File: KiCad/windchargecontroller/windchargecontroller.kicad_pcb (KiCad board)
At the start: 2 copper layers, 151.9 x 68.6 mm, 55 parts, among them J1 1935789, J2 ESQ-120-XX-X-D-XX, J3 1935789, J4 1935789, J5 1935789, J6 1935789, Q1 Si7336ADP, Q10 2N5087, Q11 Si7336ADP, Q12 Si7336ADP, Q2 Si7336ADP, Q3 Si7336ADP, Q4 2N5210, Q5 2N5087, Q6 Si7336ADP, Q7 2N5210, Q8 2N5087, Q9 2N5210

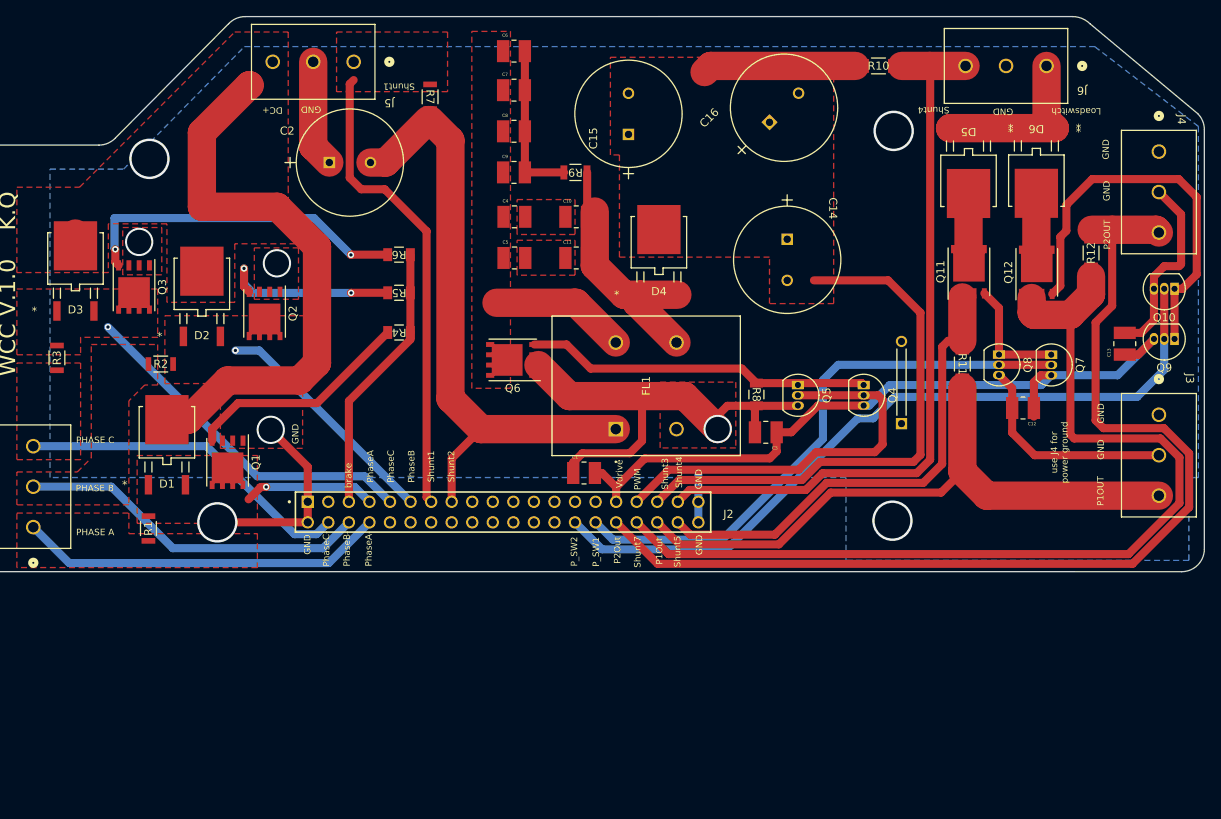
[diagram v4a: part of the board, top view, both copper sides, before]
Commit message: push before i swap out diodes for mosfets
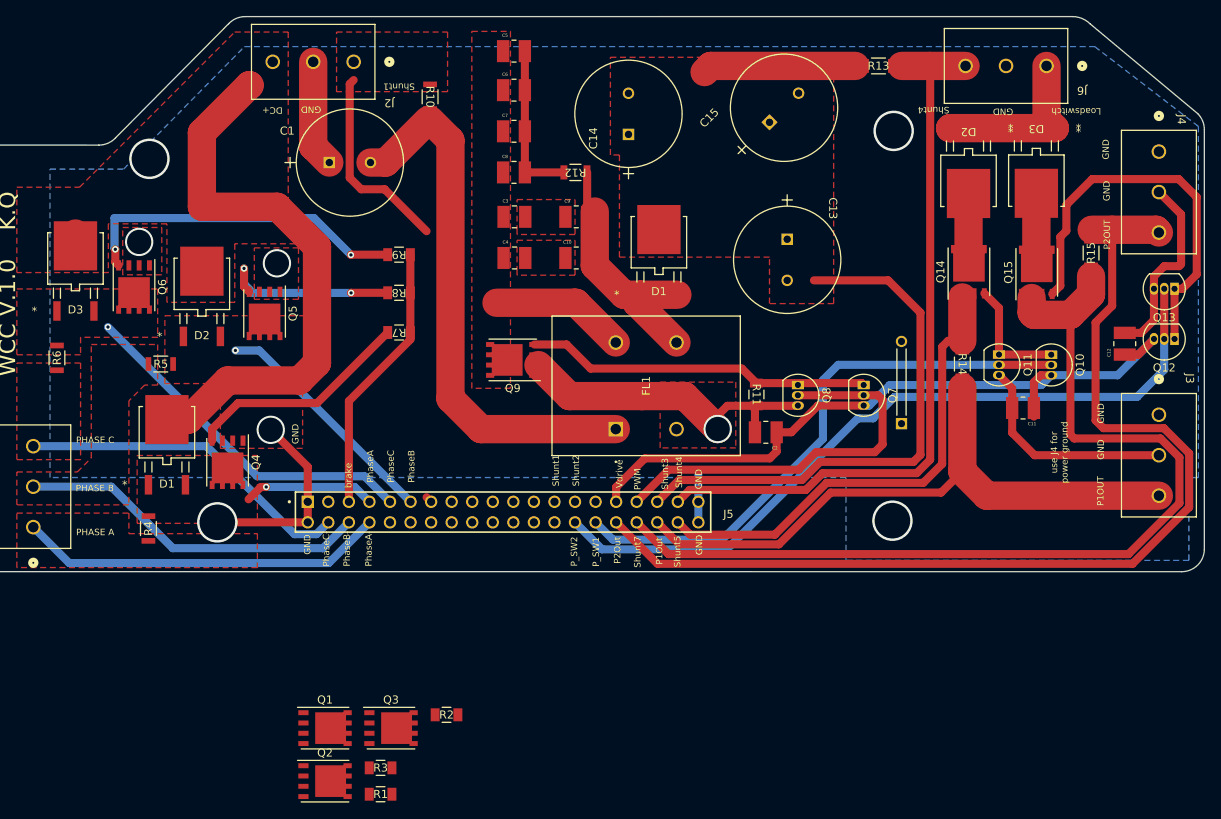
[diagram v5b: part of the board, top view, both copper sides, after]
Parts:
- removed the C1 at (148.2, 89.9)
- added Q1: Si7336ADP, Package_SO:PowerPAK_SO-8_Single, F.Cu at (116.2, 121.4)
- added Q2: Si7336ADP, Package_SO:PowerPAK_SO-8_Single, F.Cu at (116.2, 128.0)
- added Q3: Si7336ADP, Package_SO:PowerPAK_SO-8_Single, F.Cu at (124.3, 121.4)
- added R1: CRCW120616R0FKEA, footprints:RC1206N_VIS, F.Cu at (123.0, 129.6)
- added R2: CRCW120616R0FKEA, footprints:RC1206N_VIS, F.Cu at (131.2, 119.8)
- added R3: CRCW120616R0FKEA, footprints:RC1206N_VIS, F.Cu at (123.0, 126.3)
- renumbered C2 to C1, C11 to C10, C12 to C11, C13 to C12, C14 to C13, C15 to C14, C16 to C15, C3 to C2, C4 to C3, C5 to C4, C6 to C5, C7 to C6, C8 to C7, C9 to C8, C10 to C9, D4 to D1, D5 to D2, D6 to D3, J5 to J2, J2 to J5, Q7 to Q10, Q8 to Q11, Q9 to Q12, Q10 to Q13, Q11 to Q14, Q12 to Q15, Q1 to Q4, Q2 to Q5, Q3 to Q6, Q4 to Q7, Q5 to Q8, Q6 to Q9, R7 to R10, R8 to R11, R9 to R12, R10 to R13, R11 to R14, R12 to R15, R1 to R4, R2 to R5, R3 to R6, R4 to R7, R5 to R8, R6 to R9
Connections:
- J5 pad 13: Shunt1 -> Brake_Q3
- J5 pad 15: Shunt2 -> Brake_Q6
- J5 pad 17: unconnected-(J2-Pad17) -> Brake_Q2
- J5 pad 19: unconnected-(J2-Pad19) -> Brake_Q5
- J5 pad 21: unconnected-(J2-Pad21) -> Brake_Q1
- J5 pad 23: unconnected-(J2-Pad23) -> Brake_Q4
- J5 pad 25: unconnected-(J2-Pad25) -> Shunt1
- J5 pad 27: unconnected-(J2-Pad27) -> Shunt2
- R7 pad 1: Brake_sig -> Brake_Q4
- R8 pad 1: Brake_sig -> Brake_Q5
- R9 pad 1: Brake_sig -> Brake_Q6
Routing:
- net Brake_sig: track 33.7 -> 0.00 mm
- net Brake_Q6: track 0.00 -> 33.7 mm
- net Shunt1: track 58.2 -> 24.5 mm
- net GND: track 152.8 -> 136.4 mm
- net Shunt2: track 77.2 -> 66.8 mm
- net Vdrive: track 91.7 -> 88.4 mm
- net Brake_Q3: track 0.00 -> 0.79 mm
- removed copper zone on F.Cu, net Net-(C9-Pad1)

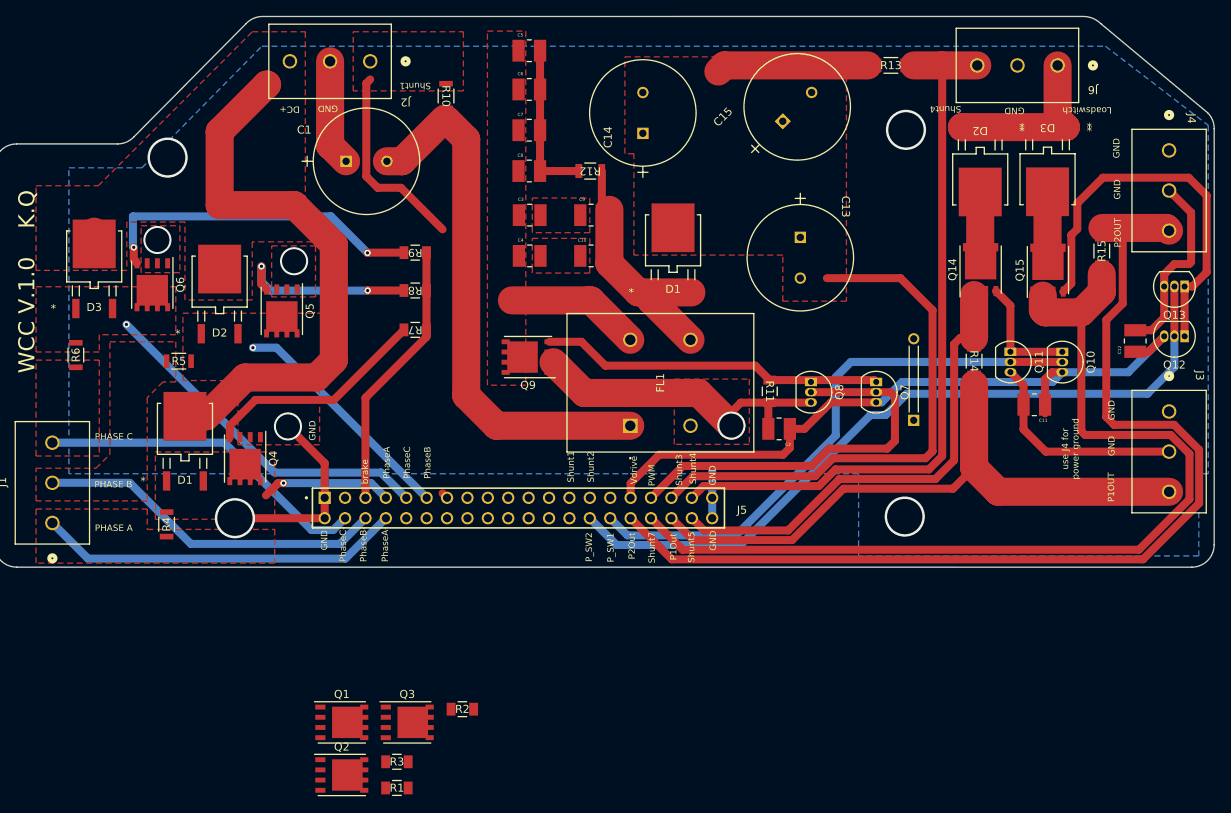
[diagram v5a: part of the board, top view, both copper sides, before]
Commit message: 6fets + DC bus
replaced rectifier diodes with mosfets for full 6 mosfet, removed their resistors due to space constraints. DC bus now directly goes into one of the power outputs + various board fixes. DRC now errorless.
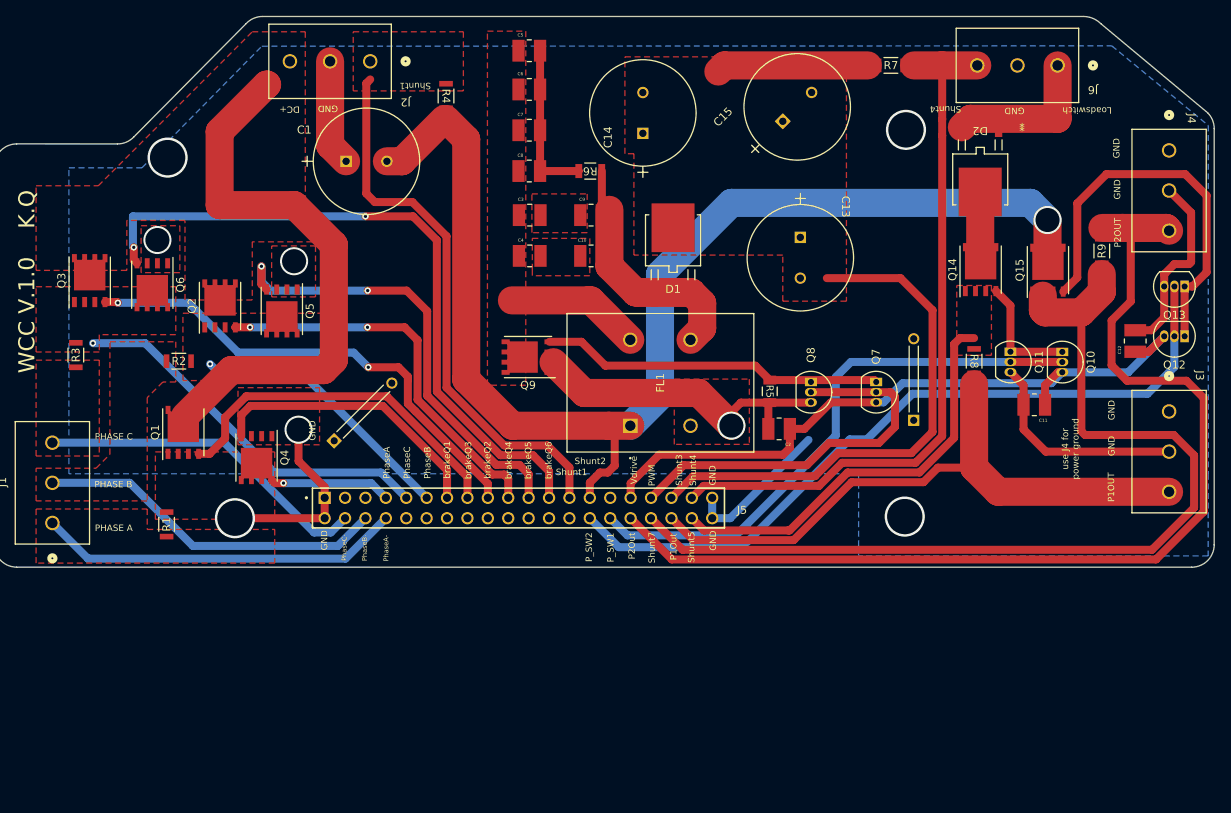
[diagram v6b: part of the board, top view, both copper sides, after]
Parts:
- removed the D1 at (96.6, 84.9)
- removed the D2 at (101.0, 66.5)
- removed D3 (x2): SBRD10200TR, footprints:DPAK_SBRD10200_6P6X6P1_SDS
- removed the R1 at (123.0, 129.6)
- removed the R2 at (131.2, 119.8)
- removed the R3 at (123.0, 126.3)
- removed the R7 at (125.3, 72.6)
- removed the R8 at (125.3, 67.7)
- removed the R9 at (125.3, 62.9)
- added REF**: STA_JW60_STP, footprints:STA_JW60_STP, F.Cu at (115.2, 86.4)
- moved Q3 67.8 mm to (84.8, 66.4), turned to 90 degrees
- moved Q2 60.3 mm to (101.0, 69.6), turned to 90 degrees
- moved Q1 41.2 mm to (96.4, 85.3), turned to 90 degrees
- moved Q4 1.43 mm to (105.6, 88.5)
- renumbered R4 to R1, R5 to R2, R6 to R3, R10 to R4, R11 to R5, R12 to R6, R13 to R7, R14 to R8, R15 to R9
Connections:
- J5 pad 05: Brake_sig -> unconnected-(J5-Pad05)
- J5 pad 13: Brake_Q3 -> Brake_Q4
- J5 pad 15: Brake_Q6 -> Brake_Q1
- J5 pad 17: Brake_Q2 -> Brake_Q3
- J5 pad 19: Brake_Q5 -> Brake_Q2
- J5 pad 21: Brake_Q1 -> Brake_Q5
- J5 pad 23: Brake_Q4 -> Brake_Q6
- Q1 pad 4: Net-(Q1-Pad4) -> Brake_Q1
- Q15 pad 5: /Q12_con -> Shunt2
- Q2 pad 4: Net-(Q2-Pad4) -> Brake_Q2
- Q3 pad 4: Net-(Q3-Pad4) -> Brake_Q3
- Q4 pad 4: /R4_con -> Brake_Q4
- Q5 pad 4: /R5_con -> Brake_Q5
- Q6 pad 4: /R6_con -> Brake_Q6
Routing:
- net Shunt2: track 66.8 -> 155.5 mm, vias 0 -> 1
- net Brake_Q3: track 0.79 -> 60.8 mm, vias 0 -> 2
- net Brake_Q5: track 0.00 -> 57.4 mm, vias 0 -> 2
- net Brake_Q6: track 33.7 -> 85.4 mm, vias 0 -> 2
- net Brake_Q2: track 0.00 -> 48.5 mm, vias 0 -> 2
- net Brake_Q1: track 0.00 -> 44.7 mm
- net Shunt1: track 24.5 -> 68.7 mm
- net /R6_con: track 41.7 -> 0.00 mm, vias 2 -> 0
- net Brake_Q4: track 0.00 -> 35.5 mm
- net /R4_con: track 28.1 -> 0.00 mm
- net /R5_con: track 23.3 -> 0.00 mm, vias 2 -> 0
- net GND: track 136.4 -> 147.0 mm
- net /Q12_con: track 9.10 -> 0.00 mm
- net Shunt5: track 59.6 -> 52.5 mm
- net /D4_con: track 32.0 -> 38.1 mm
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- added copper zone on F.Cu, net Net-(C3-Pad2)
- added copper zone on F.Cu, net Shunt5
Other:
- board text added: "brakeQ1"
- board text added: "brakeQ2"
- board text added: "brakeQ3"
- board text added: "brakeQ4"
- board text added: "brakeQ5"
- board text added: "brakeQ6"
- board text removed: "brake"

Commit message: WCC V.1.1
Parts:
- renumbered REF** to Jumper1, REF** to Jumper2
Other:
- board text added: "WCC V.1.1 K.Q"
- board text removed: "WCC V.1.0 K.Q"
- board text removed: "use J4 for power ground"
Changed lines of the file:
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@@
       (drillshape 0)
       (scaleselection 1)
-      (outputdirectory "./")
+      (outputdirectory "../output files/")
     )
   )
@@
     (tags "JW60ZT0R00 ")
     (attr through_hole)
-    (fp_text reference "REF**" (at 5.08 0 45 unlocked) (layer "F.SilkS") hide
+    (fp_text reference "Jumper2" (at 5.08 0 45 unlocked) (layer "F.SilkS") hide
       (effects (font (size 1 1) (thickness 0.15)))
     )
@@
     (tags "JW60ZT0R00 ")
     (attr through_hole)
-    (fp_text reference "REF**" (at 5.08 0 90 unlocked) (layer "F.SilkS") hide
+    (fp_text reference "Jumper1" (at 5.08 0 90 unlocked) (layer "F.SilkS") hide
       (effects (font (size 1 1) (thickness 0.15)))
     )
@@
       (effects (font (size 1 1) (thickness 0.15)))
     )
-    (fp_line (start 1.03124 0.5715) (end 9.23925 0.5715) (layer "F.SilkS") (width 0.1524))
     (fp_line (start 9.23925 -0.5715) (end 1.03124 -0.5715) (layer "F.SilkS") (width 0.1524))
-    (fp_line (start -0.9525 0.9525) (end -0.9525 -0.9525) (layer "F.CrtYd") (width 0.1524))
+    (fp_line (start 1.03124 0.5715) (end 9.23925 0.5715) (layer "F.SilkS") (width 0.1524))
     (fp_line (start 11.1125 -0.9525) (end 11.1125 0.9525) (layer "F.CrtYd") (width 0.1524))
     (fp_line (start 11.1125 0.9525) (end -0.9525 0.9525) (layer "F.CrtYd") (width 0.1524))
+    (fp_line (start -0.9525 0.9525) (end -0.9525 -0.9525) (layer "F.CrtYd") (width 0.1524))
     (fp_line (start -0.9525 -0.9525) (end 11.1125 -0.9525) (layer "F.CrtYd") (width 0.1524))
+    (fp_line (start 1.04775 -0.4445) (end 1.04775 0.4445) (layer "F.Fab") (width 0.0254))
+    (fp_line (start 9.11225 0.4445) (end 9.11225 -0.4445) (layer "F.Fab") (width 0.0254))
     (fp_line (start 9.11225 -0.4445) (end 1.04775 -0.4445) (layer "F.Fab") (width 0.0254))
     (fp_line (start 0 0) (end 1.04775 0) (layer "F.Fab") (width 0.0254))
-    (fp_line (start 9.11225 0.4445) (end 9.11225 -0.4445) (layer "F.Fab") (width 0.0254))
-    (fp_line (start 10.16 0) (end 9.11225 0) (layer "F.Fab") (width 0.0254))
-    (fp_line (start 1.04775 -0.4445) (end 1.04775 0.4445) (layer "F.Fab") (width 0.0254))
     (fp_line (start 1.04775 0.4445) (end 9.11225 0.4445) (layer "F.Fab") (width 0.0254))
+    (fp_line (start 10.16 0) (end 9.11225 0) (layer "F.Fab") (width 0.0254))
     (pad "1" thru_hole rect (at 0 0 90) (size 1.397 1.397) (drill 0.889) (layers *.Cu *.Mask)
       (net 1 "GND"))
@@
     (effects (font (size 0.8 0.8) (thickness 0.15)))
   )
-  (gr_text "use J4 for \npower ground" (at 206.9084 87.376 90) (layer "F.SilkS")
-    (effects (font (size 0.8 0.8) (thickness 0.15)))
-  )
   (gr_text "brakeQ4" (at 136.9568 88.7984 90) (layer "F.SilkS")
     (effects (font (size 0.8 0.8) (thickness 0.15)))
@@
     (effects (font (size 0.8 0.8) (thickness 0.15)))
   )
-  (gr_text "WCC V.1.0    K.Q" (at 76.962 66.548 90) (layer "F.SilkS")
+  (gr_text "WCC V.1.1    K.Q" (at 76.962 66.548 90) (layer "F.SilkS")
     (effects (font (size 2 2) (thickness 0.25)))
   )

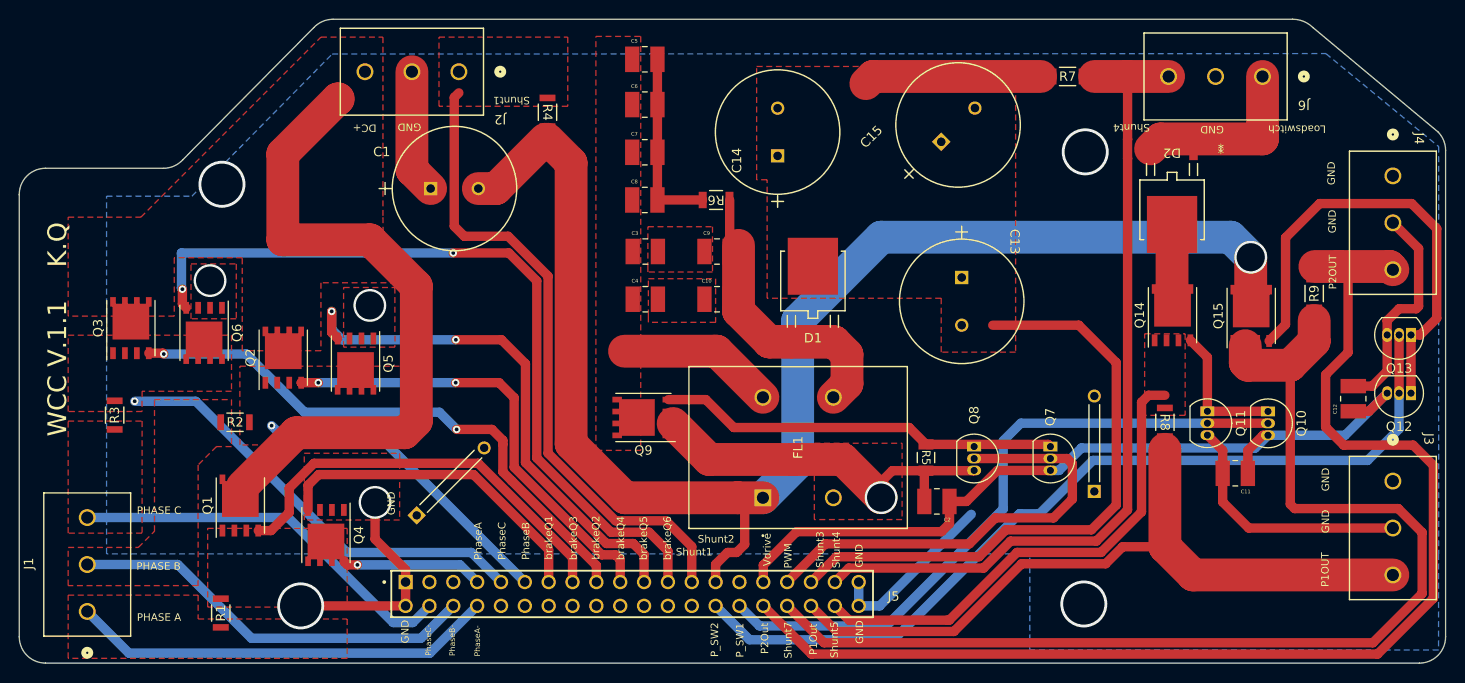
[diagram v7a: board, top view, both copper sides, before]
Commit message: updated to PCB V.1.2
made changes based on mentor's comments; mounting holes no longer grounded, reduced ground loops, moved Q12 and Q13 to allow for extra ground clearance, grounds no longer adjacent to power, and various other small fixes
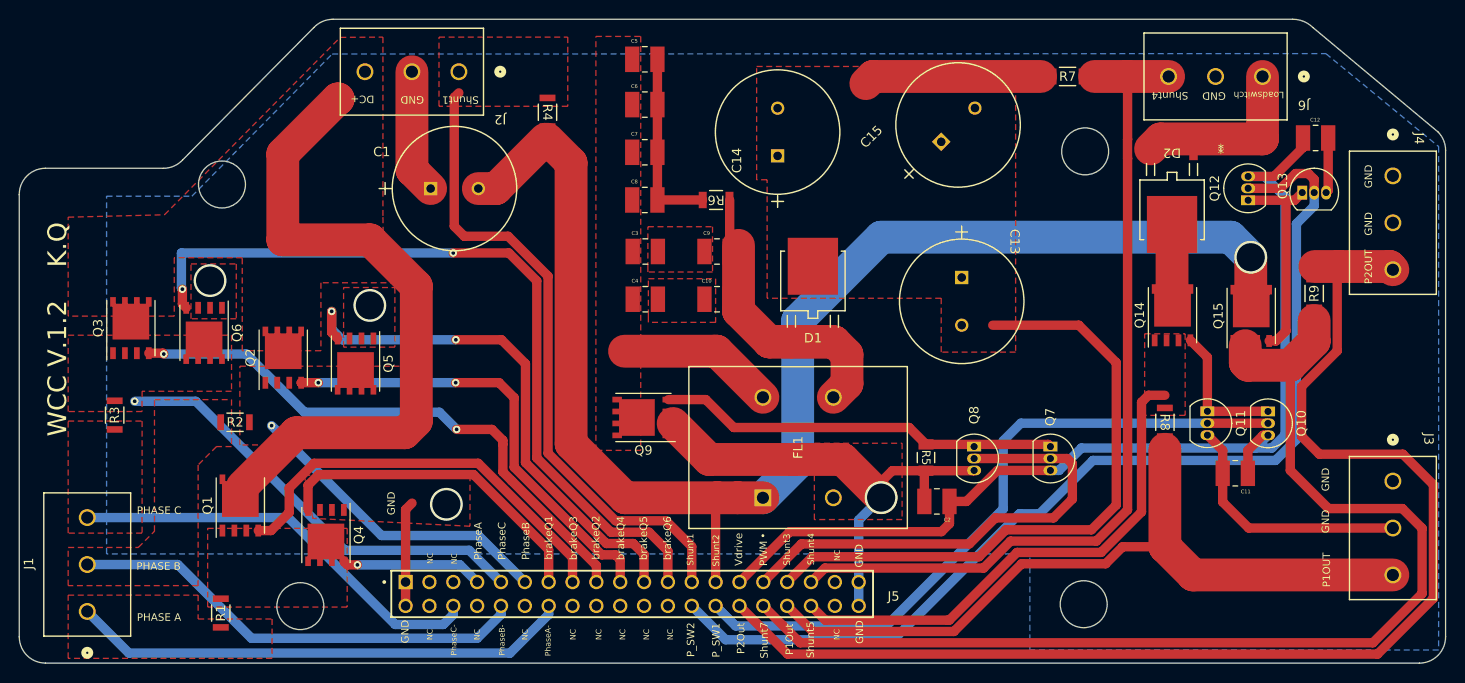
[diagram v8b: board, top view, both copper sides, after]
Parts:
- removed Jumper1, Jumper2: STA_JW60_STP, footprints:STA_JW60_STP
- moved C12 28.1 mm to (211.0, 46.2), turned to 0 degrees
- moved Q12 26.9 mm to (203.8, 52.8), turned to 90 degrees
- moved Q13 19.1 mm to (209.6, 52.0), turned to 0 degrees
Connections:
- J5 pad 04: PhaseC- -> unconnected-(J5-Pad04)
- J5 pad 06: PhaseB- -> PhaseC-
- J5 pad 08: PhaseA- -> unconnected-(J5-Pad08)
- J5 pad 10: unconnected-(J5-Pad10) -> PhaseB-
- J5 pad 14: unconnected-(J5-Pad14) -> PhaseA-
- J5 pad 26: unconnected-(J5-Pad26) -> PowerSW2
- J5 pad 28: PowerSW2 -> PowerSW1
- J5 pad 29: unconnected-(J5-Pad29) -> Vdrive
- J5 pad 30: PowerSW1 -> Power2Out
- J5 pad 31: Vdrive -> PWM_sig
- J5 pad 32: Power2Out -> Shunt7
- J5 pad 33: PWM_sig -> Shunt3
- J5 pad 34: Shunt7 -> Power1Out
- J5 pad 35: Shunt3 -> Shunt4
- J5 pad 36: Power1Out -> Shunt5
- J5 pad 37: Shunt4 -> unconnected-(J5-Pad37)
- J5 pad 38: Shunt5 -> unconnected-(J5-Pad38)
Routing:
- net GND: track 147.0 -> 110.9 mm, vias 8 -> 4
- net /Q12_drive: track 49.7 -> 22.3 mm
- net Vdrive: track 86.9 -> 111.5 mm
- net PowerSW2: track 93.6 -> 111.2 mm
- net PhaseA-: track 45.4 -> 53.6 mm
- net PhaseB-: track 43.7 -> 49.3 mm
- net Power2Out: track 130.2 -> 135.0 mm
- net PhaseC-: track 41.8 -> 45.1 mm
- net PWM_sig: track 48.5 -> 51.0 mm
- net Shunt4: track 88.4 -> 91.0 mm
- net PowerSW1: track 70.4 -> 72.9 mm
- net Shunt3: track 84.8 -> 87.4 mm
- net Power1Out: track 78.5 -> 81.0 mm
- net Shunt5: track 52.5 -> 55.1 mm
- net Shunt2: track 155.5 -> 153.5 mm
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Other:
- outline, holes or cut-outs redrawn
- board text added: "NC"
- board text added: "WCC V.1.2 K.Q"
- board text removed: "WCC V.1.1 K.Q"
